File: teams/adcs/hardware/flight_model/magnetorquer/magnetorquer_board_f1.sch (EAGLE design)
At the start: 27 parts

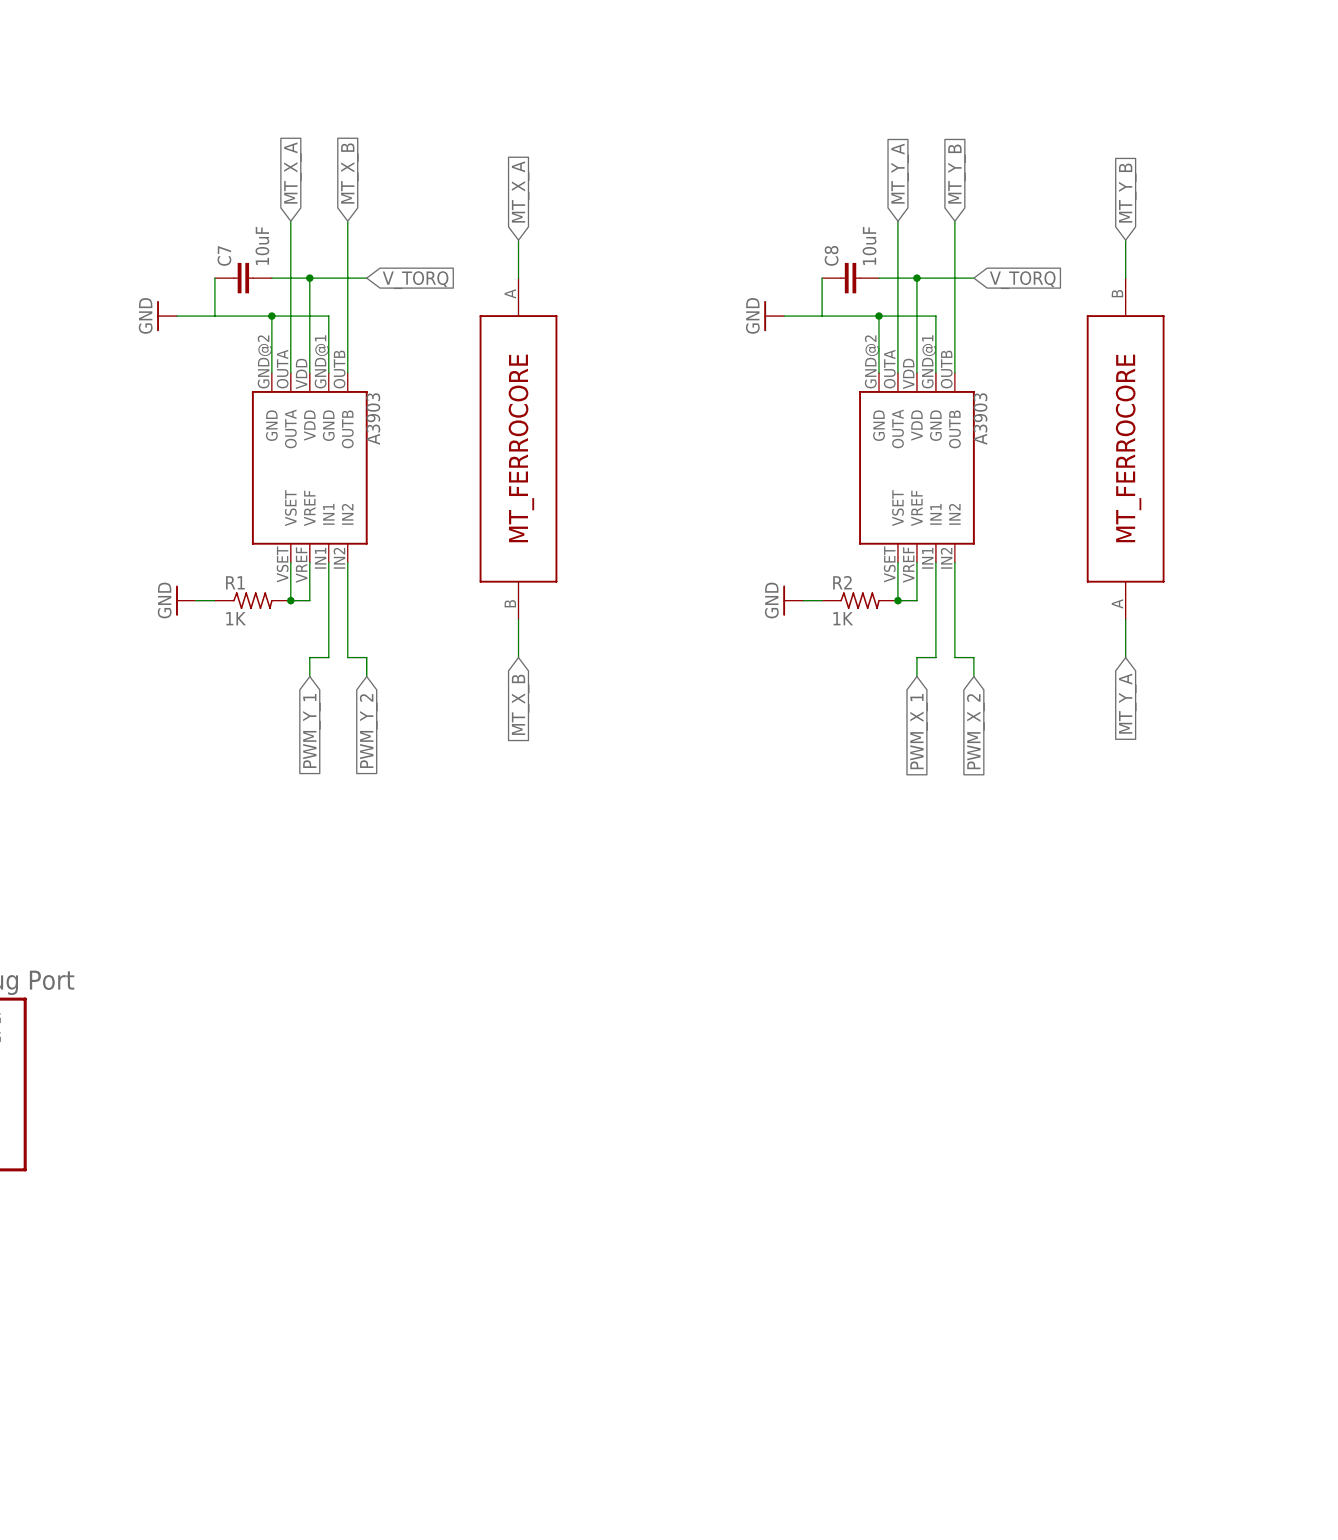
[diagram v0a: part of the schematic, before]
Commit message: ADCS/MT: Delete ferrocores
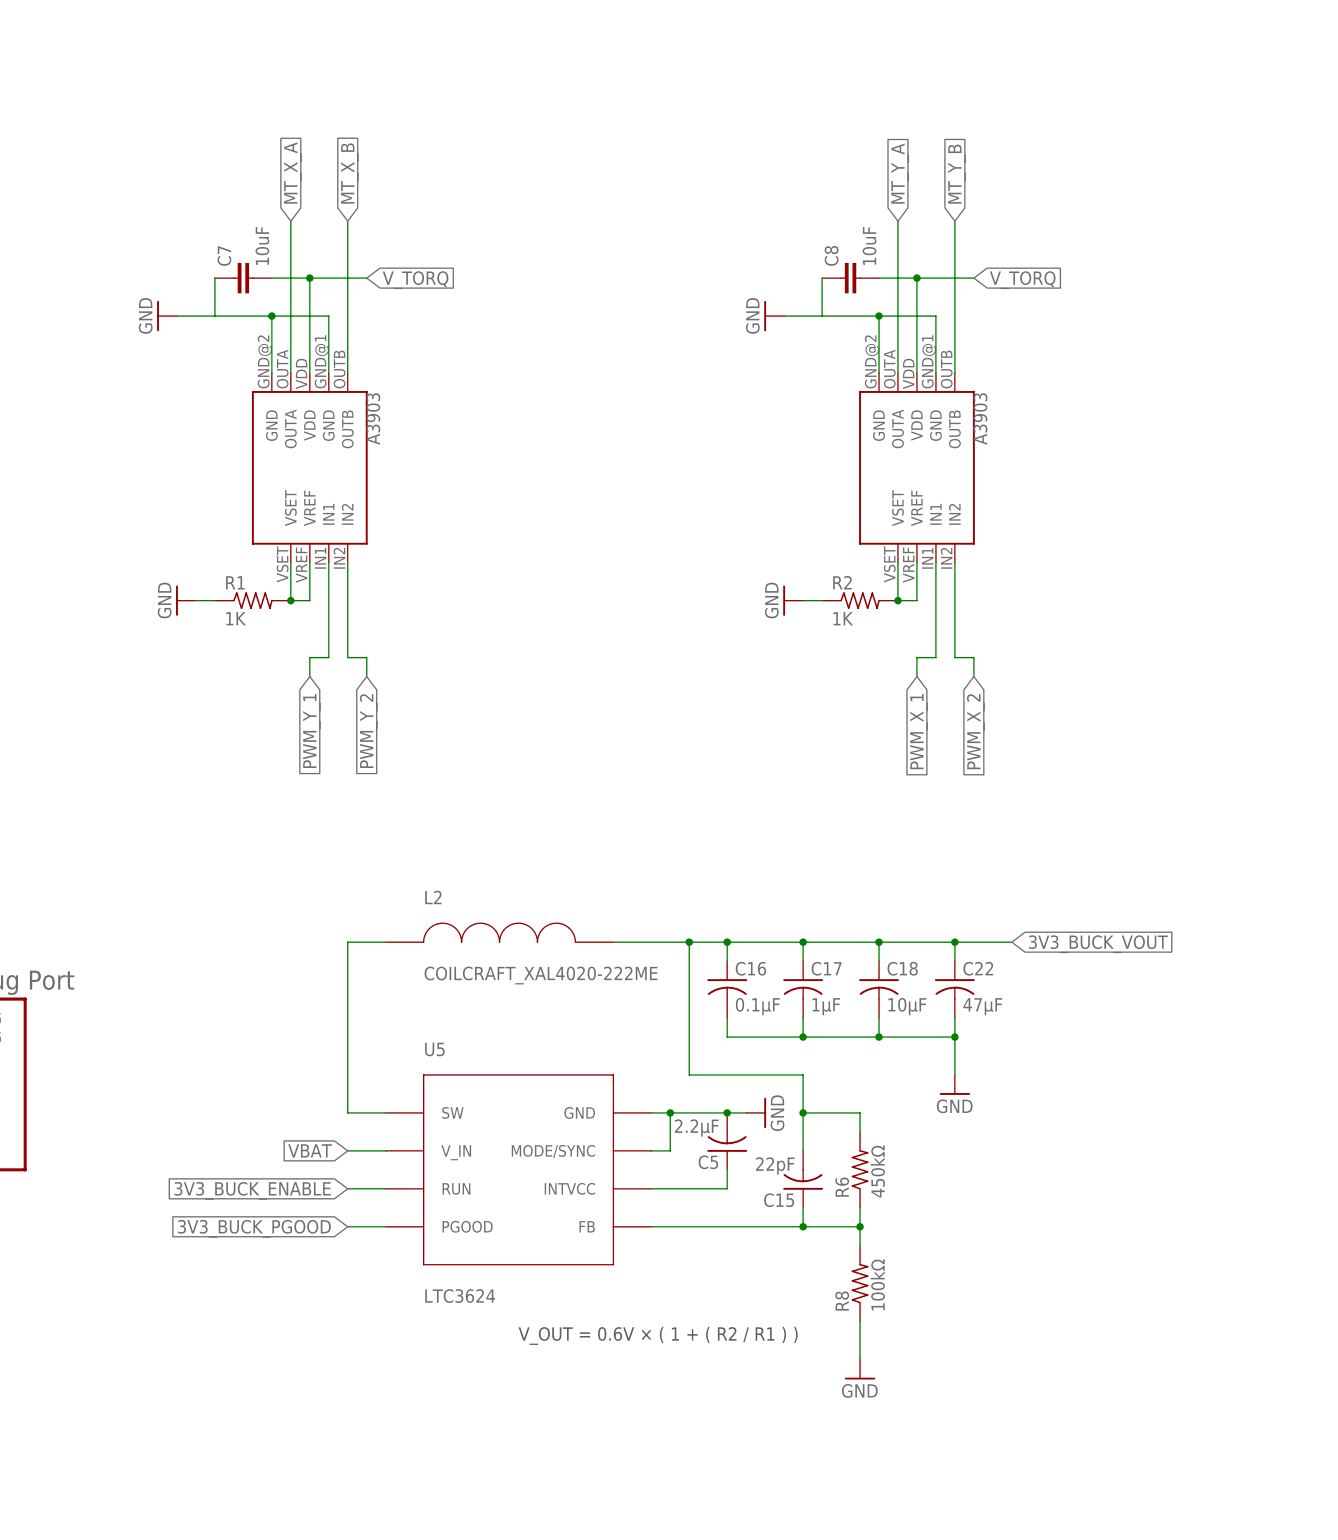
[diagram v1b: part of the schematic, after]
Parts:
- removed U$4, U$5: MT_FERROCORE, DubSat1 Components:MT_FERROCORE
- added C15: 22pF, rcl:C-USC0805
- added C16: 0.1µF, rcl:C-USC1206
- added C17: 1µF, rcl:C-USC0805
- added C18: 10µF, rcl:C-USC0805
- added C22: 47µF, rcl:C-USC0805
- added C5: 2.2μF, rcl:C-USC0805
- added L2: COILCRAFT_XAL4020-222ME, DubSat1 Components:COILCRAFT_XAL4020-222ME
- added R6: 450kΩ, rcl:R-US_R0805
- added R8: 100kΩ, rcl:R-US_R0805
- added U5: LTC3624, DubSat1 Components:LTC3624
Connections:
- new net 3V3_BUCK_ENABLE: U5.RUN
- new net 3V3_BUCK_FB1: C15.1, R6.1, R8.2, U5.FB
- new net 3V3_BUCK_INTVCC1: C5.1, U5.INTVCC
- new net 3V3_BUCK_PGOOD: U5.PGOOD
- new net 3V3_BUCK_SW1: L2.P$1, U5.SW
- new net 3V3_BUCK_VOUT: C15.2, C16.1, C17.1, C18.1, C22.1, L2.P$2, R6.2
- net GND: now also C16.2, C17.2, C18.2, C22.2, C5.2, R8.1, U5.GND, U5.MODE/SYNC
- net MT_X_A: no longer U$4.A
- net MT_X_B: no longer U$4.B
- net MT_Y_A: no longer U$5.A
- net MT_Y_B: no longer U$5.B
- net VBAT: now also U5.V_IN
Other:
- note added: "V_OUT = 0.6V × ( 1 + ( R2 / R1 ) )"

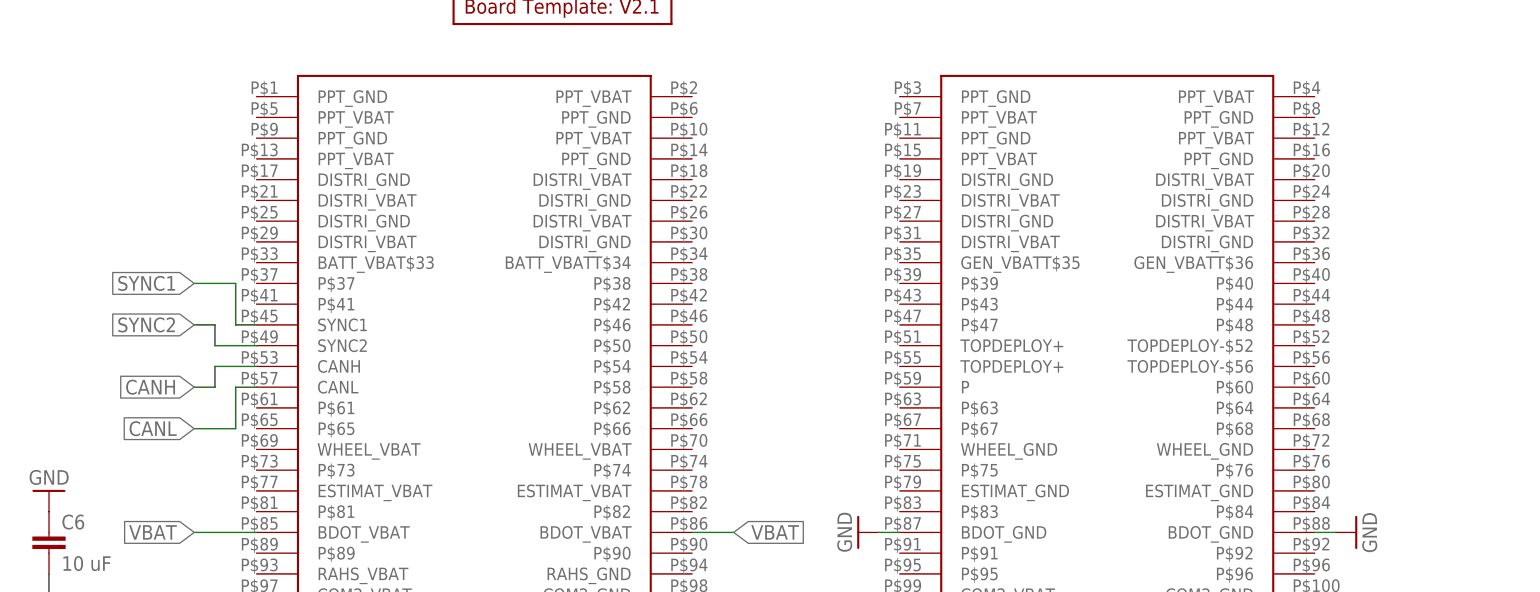
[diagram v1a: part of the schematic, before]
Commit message: ADCS/MT: Add stack hookups for X/Y aircore magnetorquers
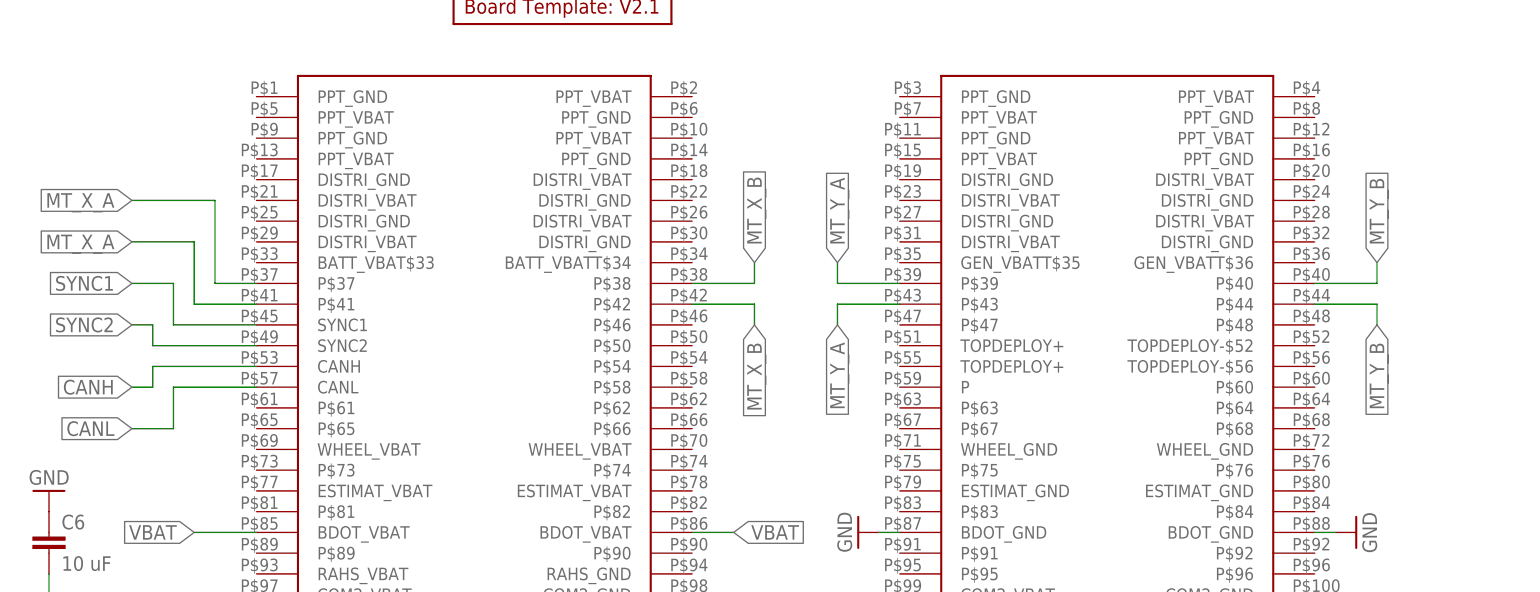
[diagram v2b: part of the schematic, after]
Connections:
- net MT_X_A: now also U$1.P$37, U$1.P$41
- net MT_X_B: now also U$1.P$38, U$1.P$42
- net MT_Y_A: now also U$1.P$39, U$1.P$43
- net MT_Y_B: now also U$1.P$40, U$1.P$44
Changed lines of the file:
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@@
 <label x="170.18" y="88.9" size="1.778" layer="95" rot="R90" xref="yes"/>
+</segment>
+<segment>
+<pinref part="U$1" gate="G$1" pin="P$42"/>
+<wire x1="30.48" y1="60.96" x2="38.1" y2="60.96" width="0.1524" layer="91"/>
+<wire x1="38.1" y1="60.96" x2="38.1" y2="58.42" width="0.1524" layer="91"/>
+<label x="38.1" y="58.42" size="1.778" layer="95" rot="R270" xref="yes"/>
+</segment>
+<segment>
+<pinref part="U$1" gate="G$1" pin="P$38"/>
+<wire x1="30.48" y1="63.5" x2="38.1" y2="63.5" width="0.1524" layer="91"/>
+<wire x1="38.1" y1="63.5" x2="38.1" y2="66.04" width="0.1524" layer="91"/>
+<label x="38.1" y="66.04" size="1.778" layer="95" rot="R90" xref="yes"/>
 </segment>
 </net>
@@
 <wire x1="162.56" y1="68.58" x2="162.56" y2="88.9" width="0.1524" layer="91"/>
 <label x="162.56" y="88.9" size="1.778" layer="95" rot="R90" xref="yes"/>
+</segment>
+<segment>
+<pinref part="U$1" gate="G$1" pin="P$41"/>
+<wire x1="-22.86" y1="60.96" x2="-30.48" y2="60.96" width="0.1524" layer="91"/>
+<wire x1="-30.48" y1="60.96" x2="-30.48" y2="68.58" width="0.1524" layer="91"/>
+<wire x1="-30.48" y1="68.58" x2="-38.1" y2="68.58" width="0.1524" layer="91"/>
+<label x="-38.1" y="68.58" size="1.778" layer="95" rot="R180" xref="yes"/>
+</segment>
+<segment>
+<pinref part="U$1" gate="G$1" pin="P$37"/>
+<wire x1="-22.86" y1="63.5" x2="-27.94" y2="63.5" width="0.1524" layer="91"/>
+<wire x1="-27.94" y1="63.5" x2="-27.94" y2="73.66" width="0.1524" layer="91"/>
+<wire x1="-27.94" y1="73.66" x2="-38.1" y2="73.66" width="0.1524" layer="91"/>
+<label x="-38.1" y="73.66" size="1.778" layer="95" rot="R180" xref="yes"/>
 </segment>
 </net>
@@
 <segment>
 <pinref part="U$1" gate="G$1" pin="CANH"/>
-<wire x1="-27.94" y1="53.34" x2="-22.86" y2="53.34" width="0.1524" layer="91"/>
-<wire x1="-27.94" y1="53.34" x2="-27.94" y2="50.8" width="0.1524" layer="91"/>
-<wire x1="-27.94" y1="50.8" x2="-30.48" y2="50.8" width="0.1524" layer="91"/>
-<label x="-30.48" y="50.8" size="1.778" layer="95" rot="R180" xref="yes"/>
+<wire x1="-35.56" y1="53.34" x2="-22.86" y2="53.34" width="0.1524" layer="91"/>
+<wire x1="-35.56" y1="53.34" x2="-35.56" y2="50.8" width="0.1524" layer="91"/>
+<wire x1="-35.56" y1="50.8" x2="-38.1" y2="50.8" width="0.1524" layer="91"/>
+<label x="-38.1" y="50.8" size="1.778" layer="95" rot="R180" xref="yes"/>
 </segment>
 <segment>
@@
 <segment>
 <pinref part="U$1" gate="G$1" pin="CANL"/>
-<wire x1="-25.4" y1="50.8" x2="-22.86" y2="50.8" width="0.1524" layer="91"/>
-<wire x1="-25.4" y1="50.8" x2="-25.4" y2="45.72" width="0.1524" layer="91"/>
-<wire x1="-25.4" y1="45.72" x2="-30.48" y2="45.72" width="0.1524" layer="91"/>
-<label x="-30.48" y="45.72" size="1.778" layer="95" rot="R180" xref="yes"/>
+<wire x1="-33.02" y1="50.8" x2="-22.86" y2="50.8" width="0.1524" layer="91"/>
+<wire x1="-33.02" y1="50.8" x2="-33.02" y2="45.72" width="0.1524" layer="91"/>
+<wire x1="-33.02" y1="45.72" x2="-38.1" y2="45.72" width="0.1524" layer="91"/>
+<label x="-38.1" y="45.72" size="1.778" layer="95" rot="R180" xref="yes"/>
 </segment>
 </net>
@@
 <segment>
 <pinref part="U$1" gate="G$1" pin="SYNC2"/>
-<wire x1="-22.86" y1="55.88" x2="-27.94" y2="55.88" width="0.1524" layer="91"/>
-<wire x1="-27.94" y1="55.88" x2="-27.94" y2="58.42" width="0.1524" layer="91"/>
-<wire x1="-27.94" y1="58.42" x2="-30.48" y2="58.42" width="0.1524" layer="91"/>
-<label x="-30.48" y="58.42" size="1.778" layer="95" rot="R180" xref="yes"/>
+<wire x1="-22.86" y1="55.88" x2="-35.56" y2="55.88" width="0.1524" layer="91"/>
+<wire x1="-35.56" y1="55.88" x2="-35.56" y2="58.42" width="0.1524" layer="91"/>
+<wire x1="-35.56" y1="58.42" x2="-38.1" y2="58.42" width="0.1524" layer="91"/>
+<label x="-38.1" y="58.42" size="1.778" layer="95" rot="R180" xref="yes"/>
 </segment>
 <segment>
@@
 <segment>
 <pinref part="U$1" gate="G$1" pin="SYNC1"/>
-<wire x1="-22.86" y1="58.42" x2="-25.4" y2="58.42" width="0.1524" layer="91"/>
-<wire x1="-25.4" y1="58.42" x2="-25.4" y2="63.5" width="0.1524" layer="91"/>
-<wire x1="-25.4" y1="63.5" x2="-30.48" y2="63.5" width="0.1524" layer="91"/>
-<label x="-30.48" y="63.5" size="1.778" layer="95" rot="R180" xref="yes"/>
+<wire x1="-22.86" y1="58.42" x2="-33.02" y2="58.42" width="0.1524" layer="91"/>
+<wire x1="-33.02" y1="58.42" x2="-33.02" y2="63.5" width="0.1524" layer="91"/>
+<wire x1="-33.02" y1="63.5" x2="-38.1" y2="63.5" width="0.1524" layer="91"/>
+<label x="-38.1" y="63.5" size="1.778" layer="95" rot="R180" xref="yes"/>
 </segment>
 <segment>
@@
 <label x="243.84" y="88.9" size="1.778" layer="95" rot="R90" xref="yes"/>
 </segment>
+<segment>
+<pinref part="U$1" gate="G$1" pin="P$39"/>
+<wire x1="55.88" y1="63.5" x2="48.26" y2="63.5" width="0.1524" layer="91"/>
+<wire x1="48.26" y1="63.5" x2="48.26" y2="66.04" width="0.1524" layer="91"/>
+<label x="48.26" y="66.04" size="1.778" layer="95" rot="R90" xref="yes"/>
+</segment>
+<segment>
+<pinref part="U$1" gate="G$1" pin="P$43"/>
+<wire x1="55.88" y1="60.96" x2="48.26" y2="60.96" width="0.1524" layer="91"/>
+<wire x1="48.26" y1="60.96" x2="48.26" y2="58.42" width="0.1524" layer="91"/>
+<label x="48.26" y="58.42" size="1.778" layer="95" rot="R270" xref="yes"/>
+</segment>
 </net>
 <net name="MT_Y_B" class="0">
@@
 <label x="251.46" y="88.9" size="1.778" layer="95" rot="R90" xref="yes"/>
 </segment>
-</net>
+<segment>
+<pinref part="U$1" gate="G$1" pin="P$44"/>
+<wire x1="106.68" y1="60.96" x2="114.3" y2="60.96" width="0.1524" layer="91"/>
+<wire x1="114.3" y1="60.96" x2="114.3" y2="58.42" width="0.1524" layer="91"/>
+<label x="114.3" y="58.42" size="1.778" layer="95" rot="R270" xref="yes"/>
+</segment>
+<segment>
+<pinref part="U$1" gate="G$1" pin="P$40"/>
+<wire x1="106.68" y1="63.5" x2="114.3" y2="63.5" width="0.1524" layer="91"/>
+<wire x1="114.3" y1="63.5" x2="114.3" y2="66.04" width="0.1524" layer="91"/>
+<label x="114.3" y="66.04" size="1.778" layer="95" rot="R90" xref="yes"/>
+</segment>
+</net>
